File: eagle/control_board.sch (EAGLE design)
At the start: 24 parts, among them Q1 TIP122V

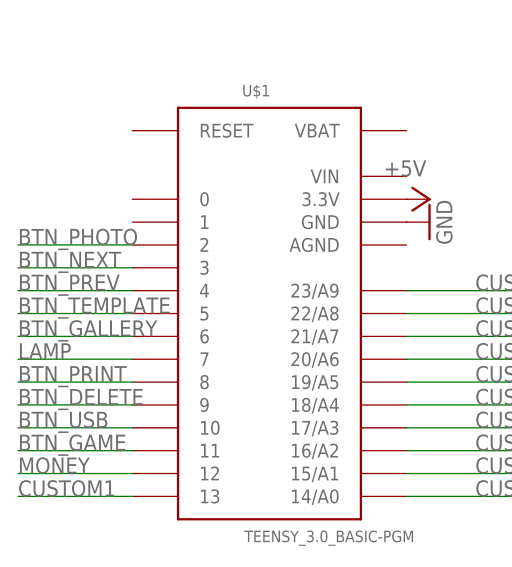
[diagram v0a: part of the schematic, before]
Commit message: Working form & light control
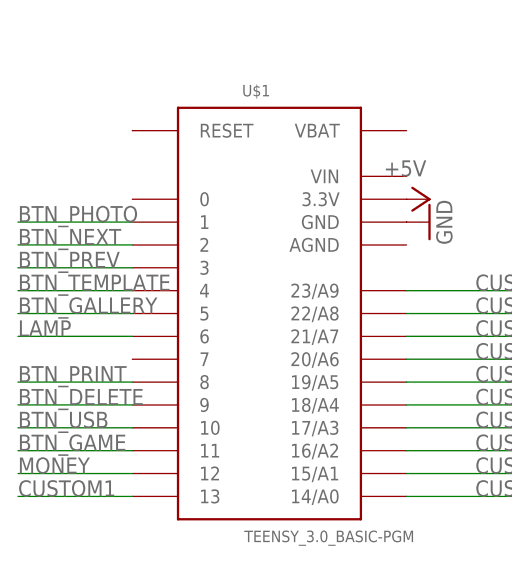
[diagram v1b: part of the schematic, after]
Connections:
- net BTN_GALLERY: now also U$1.5; no longer U$1.6
- net BTN_NEXT: now also U$1.2; no longer U$1.3
- net BTN_PHOTO: now also U$1.1; no longer U$1.2
- net BTN_PREV: now also U$1.3; no longer U$1.4
- net BTN_TEMPLATE: now also U$1.4; no longer U$1.5
- net LAMP: now also U$1.6; no longer U$1.7
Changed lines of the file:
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@@
 <net name="BTN_PHOTO" class="0">
-<segment>
-<pinref part="U$1" gate="G$1" pin="2"/>
-<wire x1="-43.18" y1="66.04" x2="-55.88" y2="66.04" width="0.1524" layer="91"/>
-<label x="-55.88" y="66.04" size="1.778" layer="95"/>
-</segment>
 <segment>
 <pinref part="FRONT-CONTROL" gate="-3" pin="S"/>
@@
 <junction x="101.6" y="96.52"/>
 </segment>
+<segment>
+<pinref part="U$1" gate="G$1" pin="1"/>
+<wire x1="-43.18" y1="68.58" x2="-55.88" y2="68.58" width="0.1524" layer="91"/>
+<label x="-55.88" y="68.58" size="1.778" layer="95"/>
+</segment>
 </net>
 <net name="BTN_NEXT" class="0">
-<segment>
-<pinref part="U$1" gate="G$1" pin="3"/>
-<wire x1="-43.18" y1="63.5" x2="-55.88" y2="63.5" width="0.1524" layer="91"/>
-<label x="-55.88" y="63.5" size="1.778" layer="95"/>
-</segment>
 <segment>
 <pinref part="FRONT-CONTROL" gate="-4" pin="S"/>
@@
 <junction x="116.84" y="91.44"/>
 </segment>
+<segment>
+<pinref part="U$1" gate="G$1" pin="2"/>
+<wire x1="-43.18" y1="66.04" x2="-55.88" y2="66.04" width="0.1524" layer="91"/>
+<label x="-55.88" y="66.04" size="1.778" layer="95"/>
+</segment>
 </net>
 <net name="BTN_PREV" class="0">
-<segment>
-<pinref part="U$1" gate="G$1" pin="4"/>
-<wire x1="-43.18" y1="60.96" x2="-55.88" y2="60.96" width="0.1524" layer="91"/>
-<label x="-55.88" y="60.96" size="1.778" layer="95"/>
-</segment>
 <segment>
 <pinref part="FRONT-CONTROL" gate="-5" pin="S"/>
@@
 <junction x="132.08" y="86.36"/>
 </segment>
+<segment>
+<pinref part="U$1" gate="G$1" pin="3"/>
+<wire x1="-43.18" y1="63.5" x2="-55.88" y2="63.5" width="0.1524" layer="91"/>
+<label x="-55.88" y="63.5" size="1.778" layer="95"/>
+</segment>
 </net>
 <net name="BTN_TEMPLATE" class="0">
-<segment>
-<pinref part="U$1" gate="G$1" pin="5"/>
-<wire x1="-43.18" y1="58.42" x2="-55.88" y2="58.42" width="0.1524" layer="91"/>
-<label x="-55.88" y="58.42" size="1.778" layer="95"/>
-</segment>
 <segment>
 <pinref part="FRONT-CONTROL" gate="-6" pin="S"/>
@@
 <junction x="147.32" y="81.28"/>
 </segment>
+<segment>
+<pinref part="U$1" gate="G$1" pin="4"/>
+<wire x1="-43.18" y1="60.96" x2="-55.88" y2="60.96" width="0.1524" layer="91"/>
+<label x="-55.88" y="60.96" size="1.778" layer="95"/>
+</segment>
 </net>
 <net name="BTN_GALLERY" class="0">
-<segment>
-<pinref part="U$1" gate="G$1" pin="6"/>
-<wire x1="-43.18" y1="55.88" x2="-55.88" y2="55.88" width="0.1524" layer="91"/>
-<label x="-55.88" y="55.88" size="1.778" layer="95"/>
-</segment>
 <segment>
 <pinref part="FRONT-CONTROL" gate="-7" pin="S"/>
@@
 <junction x="162.56" y="76.2"/>
 </segment>
+<segment>
+<pinref part="U$1" gate="G$1" pin="5"/>
+<wire x1="-43.18" y1="58.42" x2="-55.88" y2="58.42" width="0.1524" layer="91"/>
+<label x="-55.88" y="58.42" size="1.778" layer="95"/>
+</segment>
 </net>
 <net name="BTN_PRINT" class="0">
@@
 </segment>
 <segment>
-<pinref part="U$1" gate="G$1" pin="7"/>
-<wire x1="-43.18" y1="53.34" x2="-55.88" y2="53.34" width="0.1524" layer="91"/>
-<label x="-55.88" y="53.34" size="1.778" layer="95"/>
-</segment>
-</net>
+<pinref part="U$1" gate="G$1" pin="6"/>
+<wire x1="-43.18" y1="55.88" x2="-55.88" y2="55.88" width="0.1524" layer="91"/>
+<label x="-55.88" y="55.88" size="1.778" layer="95"/>
+</segment>
+</net>
